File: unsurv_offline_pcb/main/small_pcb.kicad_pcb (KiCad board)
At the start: 4 copper layers, 35 x 45 mm, 51 parts, among them J1 USB_B_Micro, Q1 Q_PMOS_GSD, Q2 UMH3N, SW1 SW_DIP_x01, U1 MCP73831-2-OT, U2 AP2112K-3.3, U3 MPU-6050_NRND, U4 ESP32-WROOM-32, U5 RF430CL330H, U6 CAM-M8C-0-10, U7 CH340G

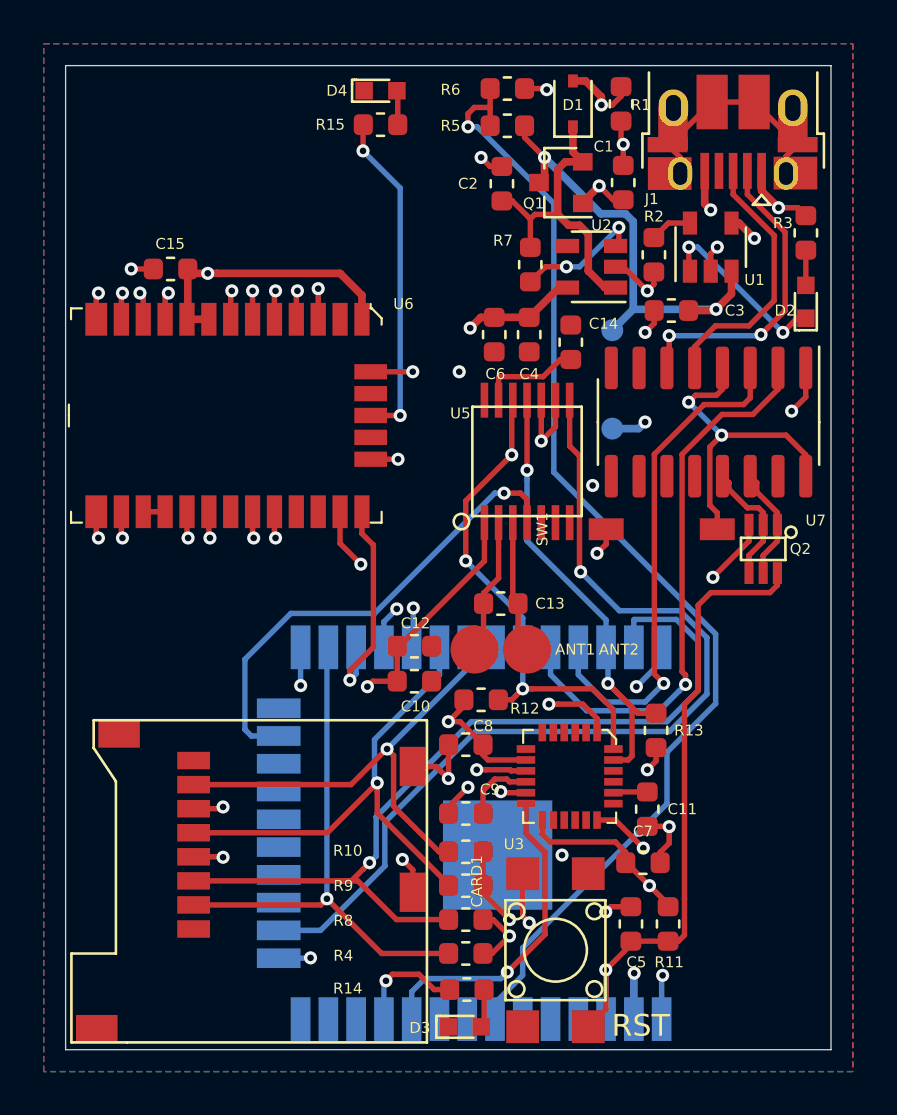
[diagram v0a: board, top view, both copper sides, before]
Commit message: lowered power consumption in deep sleep
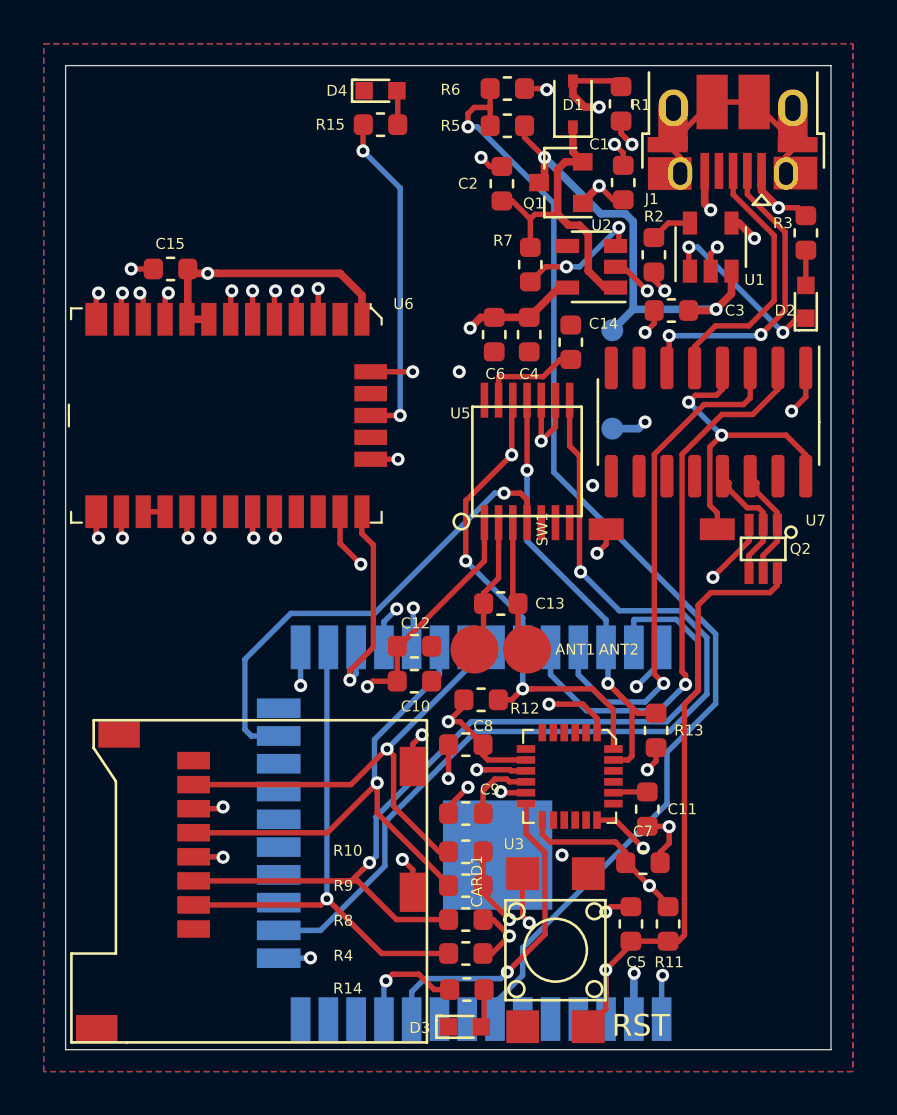
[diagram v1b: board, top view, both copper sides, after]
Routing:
- net +5V: track 10.7 -> 11.6 mm
- net GND: track 67.9 -> 68.1 mm, vias 42 -> 45
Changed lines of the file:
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@@
     (thickness 1.6)
     (drawings 12)
-    (tracks 610)
+    (tracks 613)
     (zones 0)
     (modules 51)
@@
   (layers
     (0 F.Cu signal)
-    (1 GND power hide)
-    (2 PWR power hide)
+    (1 GND power)
+    (2 PWR power)
     (31 B.Cu signal)
     (32 B.Adhes user hide)
@@
     (tags capacitor)
     (attr smd)
-    (fp_text reference C1 (at -1.65 0.9 180) (layer F.SilkS)
+    (fp_text reference C1 (at -1.75 1.1 180) (layer F.SilkS)
       (effects (font (size 0.5 0.5) (thickness 0.1)))
     )
@@
   (segment (start 69.95 54.6125) (end 69.4125 54.6125) (width 0.25) (layer F.Cu) (net 1))
   (segment (start 69.4125 54.6125) (end 69 54.2) (width 0.25) (layer F.Cu) (net 1))
-  (via (at 75.5 53.6) (size 0.6) (drill 0.3) (layers F.Cu B.Cu) (net 1))
-  (segment (start 75.5 54.5625) (end 75.5 53.6) (width 0.25) (layer F.Cu) (net 1))
-  (segment (start 75.4 53.5) (end 75.5 53.6) (width 0.25) (layer F.Cu) (net 1))
-  (segment (start 75.4 52.5375) (end 75.4 53.5) (width 0.25) (layer F.Cu) (net 1))
   (segment (start 79.225 54.815) (end 79.225 56.325) (width 0.35) (layer F.Cu) (net 1))
   (via (at 79.5 56.6) (size 0.6) (drill 0.3) (layers F.Cu B.Cu) (net 1))
@@
   (segment (start 76.9125 61.7875) (end 76.5 62.2) (width 0.25) (layer F.Cu) (net 1))
   (via (at 76.6 60.3) (size 0.6) (drill 0.3) (layers F.Cu B.Cu) (net 1))
-  (segment (start 76.9 59.4375) (end 76.9 60) (width 0.25) (layer F.Cu) (net 1))
-  (segment (start 76.9 60) (end 76.6 60.3) (width 0.25) (layer F.Cu) (net 1))
   (segment (start 75.5 59.2) (end 76.6 60.3) (width 0.25) (layer F.Cu) (net 1))
   (segment (start 75.15 59.2) (end 75.5 59.2) (width 0.25) (layer F.Cu) (net 1))
@@
   (segment (start 67.5125 81.05) (end 67.5125 82.587478) (width 0.25) (layer F.Cu) (net 1))
   (segment (start 67.5125 82.587478) (end 67.5 82.599978) (width 0.25) (layer F.Cu) (net 1))
-  (segment (start 67.200001 82.299979) (end 67.5 82.599978) (width 0.25) (layer F.Cu) (net 1))
-  (segment (start 66.950022 82.05) (end 67.200001 82.299979) (width 0.25) (layer F.Cu) (net 1))
-  (segment (start 65.875 82.05) (end 66.950022 82.05) (width 0.25) (layer F.Cu) (net 1))
   (via (at 69.9 83.2) (size 0.6) (drill 0.3) (layers F.Cu B.Cu) (net 1))
   (segment (start 71.05 83.25) (end 69.95 83.25) (width 0.25) (layer F.Cu) (net 1))
@@
   (segment (start 67.5125 84.2) (end 67.5125 83.8875) (width 0.25) (layer F.Cu) (net 1))
   (segment (start 67.5125 83.8875) (end 68.4 83) (width 0.25) (layer F.Cu) (net 1))
+  (segment (start 75.4 53.1) (end 75.600001 53.300001) (width 0.25) (layer F.Cu) (net 1))
+  (segment (start 75.600001 53.300001) (end 75.9 53.6) (width 0.25) (layer F.Cu) (net 1))
+  (via (at 75.9 53.6) (size 0.6) (drill 0.3) (layers F.Cu B.Cu) (net 1))
+  (segment (start 75.4 52.5375) (end 75.4 53.1) (width 0.25) (layer F.Cu) (net 1))
+  (via (at 75.1 53.6) (size 0.6) (drill 0.3) (layers F.Cu B.Cu) (net 1))
+  (segment (start 75.5 54) (end 75.1 53.6) (width 0.25) (layer F.Cu) (net 1))
+  (segment (start 75.5 54.5625) (end 75.5 54) (width 0.25) (layer F.Cu) (net 1))
+  (via (at 77.4 60.3) (size 0.6) (drill 0.3) (layers F.Cu B.Cu) (net 1))
+  (segment (start 76.9 59.4375) (end 76.9 59.8) (width 0.25) (layer F.Cu) (net 1))
+  (segment (start 76.9 59.8) (end 77.4 60.3) (width 0.25) (layer F.Cu) (net 1))
+  (via (at 66.3 80.6) (size 0.6) (drill 0.3) (layers F.Cu B.Cu) (net 1))
+  (segment (start 65.875 82.05) (end 65.875 81.025) (width 0.25) (layer F.Cu) (net 1))
+  (segment (start 65.875 81.025) (end 66.3 80.6) (width 0.25) (layer F.Cu) (net 1))
   (via (at 82.6 56.5) (size 0.6) (drill 0.3) (layers F.Cu B.Cu) (net 2))
   (segment (start 81.825 54.815) (end 81.825 55.725) (width 0.35) (layer F.Cu) (net 2))
@@
   (segment (start 83.4875 56.5) (end 83.85 56.8625) (width 0.25) (layer F.Cu) (net 2))
   (segment (start 82.6 56.5) (end 83.4875 56.5) (width 0.25) (layer F.Cu) (net 2))
-  (via (at 74.499998 51.8) (size 0.6) (drill 0.3) (layers F.Cu B.Cu) (net 2))
-  (segment (start 73.2 50.7) (end 73.775 50.7) (width 0.35) (layer F.Cu) (net 2))
-  (segment (start 75.4 51.4) (end 75 51.8) (width 0.25) (layer F.Cu) (net 2))
-  (segment (start 75 51.8) (end 74.499998 51.8) (width 0.25) (layer F.Cu) (net 2))
-  (segment (start 74.499998 51.424998) (end 74.499998 51.8) (width 0.35) (layer F.Cu) (net 2))
-  (segment (start 73.775 50.7) (end 74.499998 51.424998) (width 0.35) (layer F.Cu) (net 2))
-  (segment (start 75.4 50.9625) (end 75.4 51.4) (width 0.25) (layer F.Cu) (net 2))
+  (segment (start 75.1375 50.7) (end 75.4 50.9625) (width 0.25) (layer F.Cu) (net 2))
+  (segment (start 73.2 50.7) (end 75.1375 50.7) (width 0.25) (layer F.Cu) (net 2))
+  (via (at 74.4 51.9) (size 0.6) (drill 0.3) (layers F.Cu B.Cu) (net 2))
+  (segment (start 73.75 51.9) (end 74.4 51.9) (width 0.35) (layer F.Cu) (net 2))
+  (segment (start 73.2 50.7) (end 73.2 51.35) (width 0.35) (layer F.Cu) (net 2))
+  (segment (start 73.2 51.35) (end 73.75 51.9) (width 0.35) (layer F.Cu) (net 2))
   (segment (start 79.6875 61.2) (end 78.4875 61.2) (width 0.35) (layer F.Cu) (net 3))
   (segment (start 80.45 59.4) (end 80.45 60.4375) (width 0.35) (layer F.Cu) (net 3))

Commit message: updated 3D files + exported schematic
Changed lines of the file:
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@@
     (thickness 1.6)
     (drawings 12)
-    (tracks 613)
+    (tracks 616)
     (zones 0)
     (modules 51)
@@
   )
   (setup
-    (last_trace_width 0.25)
+    (last_trace_width 0.35)
     (user_trace_width 0.35)
     (user_trace_width 0.5)
@@
   (segment (start 79.74375 61.14375) (end 79.6875 61.2) (width 0.35) (layer F.Cu) (net 3))
   (via (at 79.74375 61.14375) (size 0.6) (drill 0.3) (layers F.Cu B.Cu) (net 3))
-  (segment (start 75.95625 61.14375) (end 79.74375 61.14375) (width 0.35) (layer B.Cu) (net 3))
-  (segment (start 75 62.1) (end 75.95625 61.14375) (width 0.35) (layer B.Cu) (net 3))
   (via (at 71.9 54.2) (size 0.6) (drill 0.3) (layers F.Cu B.Cu) (net 3))
-  (segment (start 75.600001 56.774999) (end 74.474999 56.774999) (width 0.35) (layer B.Cu) (net 3))
-  (segment (start 75.95625 61.14375) (end 75.95625 57.131248) (width 0.35) (layer B.Cu) (net 3))
-  (segment (start 74.474999 56.774999) (end 71.9 54.2) (width 0.35) (layer B.Cu) (net 3))
-  (segment (start 75.95625 57.131248) (end 75.600001 56.774999) (width 0.35) (layer B.Cu) (net 3))
   (segment (start 71.9 55.1) (end 71.65 55.35) (width 0.35) (layer F.Cu) (net 3))
   (segment (start 71.9 54.2) (end 71.9 55.1) (width 0.35) (layer F.Cu) (net 3))
   (segment (start 70.9875 53.2875) (end 71.9 54.2) (width 0.25) (layer F.Cu) (net 3))
   (segment (start 70.9875 52.75) (end 70.9875 53.2875) (width 0.25) (layer F.Cu) (net 3))
+  (segment (start 76.518748 61.14375) (end 79.74375 61.14375) (width 0.35) (layer B.Cu) (net 3))
+  (segment (start 74.474999 56.774999) (end 75.600001 56.774999) (width 0.35) (layer B.Cu) (net 3))
+  (segment (start 71.9 54.2) (end 74.474999 56.774999) (width 0.35) (layer B.Cu) (net 3))
+  (segment (start 75.600001 56.774999) (end 75.95625 57.131248) (width 0.35) (layer B.Cu) (net 3))
+  (segment (start 75.95625 57.131248) (end 75.95625 60.581252) (width 0.35) (layer B.Cu) (net 3))
+  (segment (start 75.95625 60.581252) (end 76.518748 61.14375) (width 0.35) (layer B.Cu) (net 3))
+  (segment (start 75.811642 60.581252) (end 75.95625 60.581252) (width 0.35) (layer B.Cu) (net 3))
+  (segment (start 75 61.392894) (end 75.811642 60.581252) (width 0.35) (layer B.Cu) (net 3))
+  (segment (start 75 62.1) (end 75 61.392894) (width 0.35) (layer B.Cu) (net 3))
   (segment (start 69.0875 81.525) (end 69.0875 81.05) (width 0.25) (layer F.Cu) (net 4))
   (segment (start 69.3125 81.75) (end 69.0875 81.525) (width 0.25) (layer F.Cu) (net 4))
